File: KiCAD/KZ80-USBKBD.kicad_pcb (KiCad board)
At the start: 2 copper layers, 100 x 75 mm, 33 parts, among them J1 SBC8080 BUS, J2 CON-A, J3 CMT-OUT, J4 232C(DEBUG), J5 ADR-JP2, J6 ADR-JP1, SW1 SW_SPST, U1 Pico, U2 8255, U3 74HC139, U4 74HC00

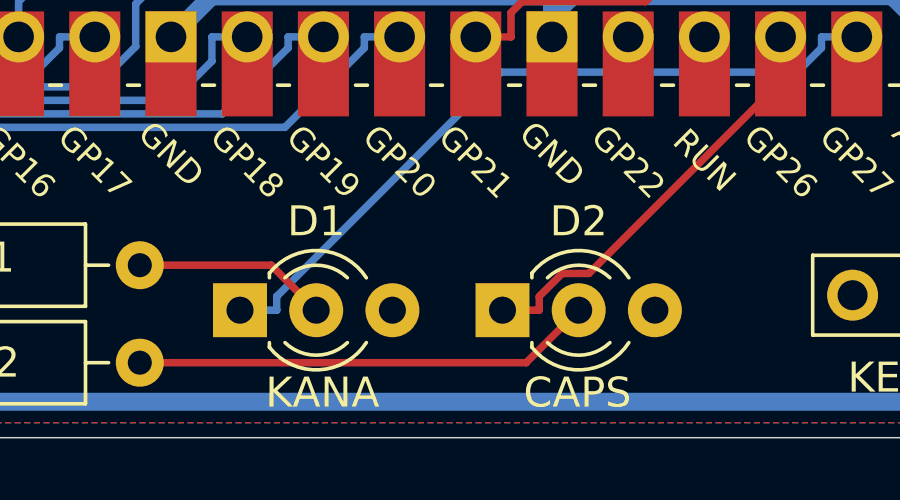
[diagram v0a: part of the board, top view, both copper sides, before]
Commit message: LEDフットプリント間違い修正
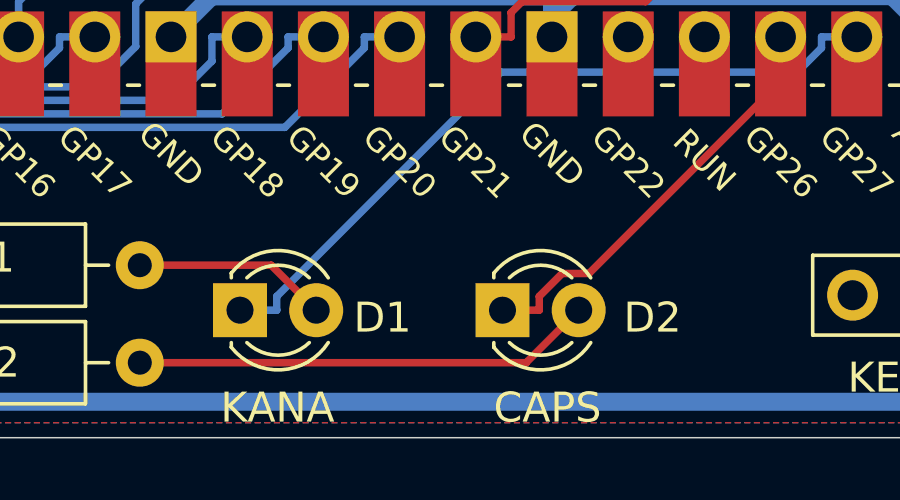
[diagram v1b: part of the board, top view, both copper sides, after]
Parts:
- D1, D2: footprint LED_THT:LED_D3.0mm-3 -> LED_THT:LED_D3.0mm
- R6, R7, R8, R9: value 1k -> 10k
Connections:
- J1 pad 18: Net-(J1-Pad18) -> (no net)
- J1 pad 20: Net-(J1-Pad20) -> (no net)
- J1 pad 22: Net-(J1-Pad22) -> (no net)
- J1 pad 23: Net-(J1-Pad23) -> (no net)
- J1 pad 24: Net-(J1-Pad24) -> (no net)
- J1 pad 27: Net-(J1-Pad27) -> (no net)
- J1 pad 33: Net-(J1-Pad33) -> (no net)
- J1 pad 34: Net-(J1-Pad34) -> (no net)
- J1 pad 35: Net-(J1-Pad35) -> (no net)
- J1 pad 36: Net-(J1-Pad36) -> (no net)
- J1 pad 37: Net-(J1-Pad37) -> (no net)
- J1 pad 38: Net-(J1-Pad38) -> (no net)
- J1 pad 39: Net-(J1-Pad39) -> (no net)
- J1 pad 40: Net-(J1-Pad40) -> (no net)
- J1 pad 5: Net-(J1-Pad5) -> (no net)
- J1 pad 6: Net-(J1-Pad6) -> (no net)
- J1 pad 7: Net-(J1-Pad7) -> (no net)
- J1 pad 8: Net-(J1-Pad8) -> (no net)
- J3 pad 2: Net-(J3-Pad2) -> (no net)
- J3 pad 3: Net-(J3-Pad3) -> (no net)
- J3 pad 4: Net-(J3-Pad4) -> (no net)
- J4 pad 2: Net-(J4-Pad2) -> (no net)
- J4 pad 3: Net-(J4-Pad3) -> (no net)
- J4 pad 6: Net-(J4-Pad6) -> (no net)

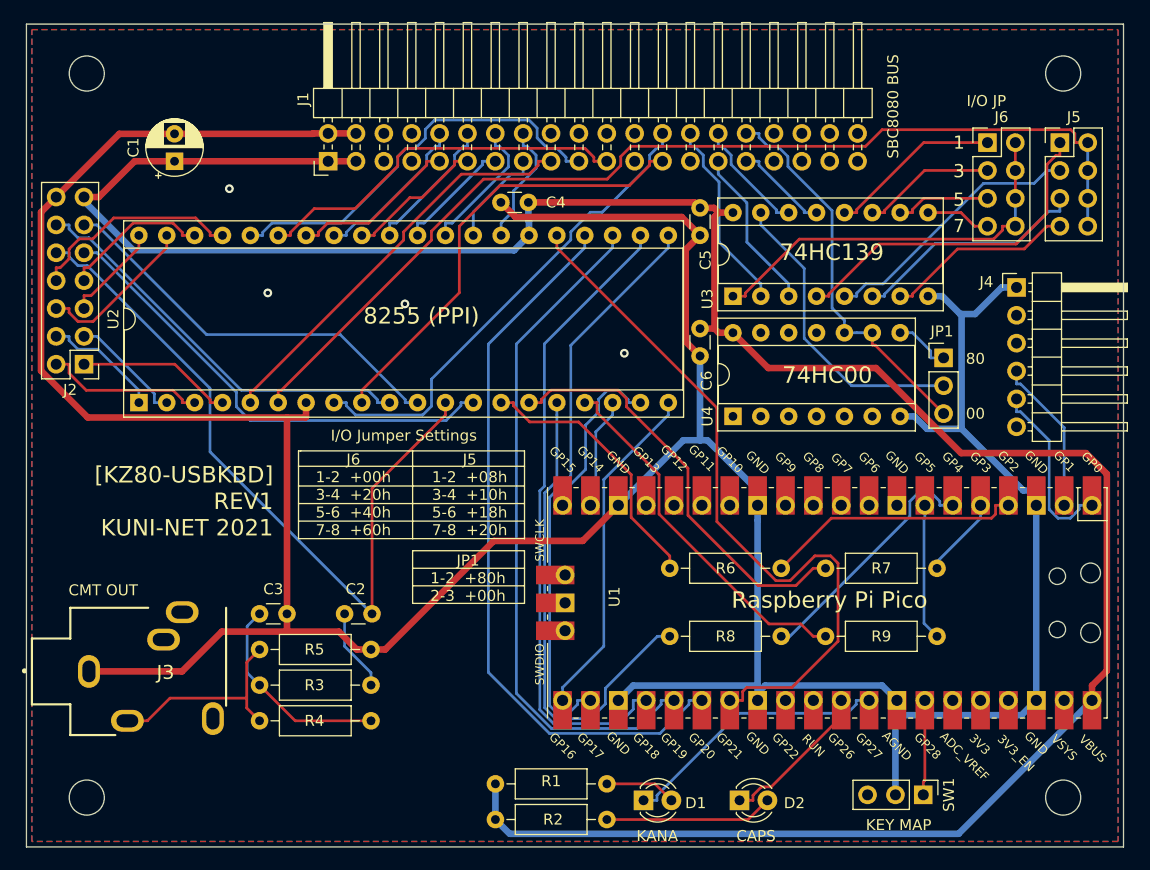
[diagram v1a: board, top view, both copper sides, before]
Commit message: REV1基板バグ対応、REV2作成、ガーバー出力
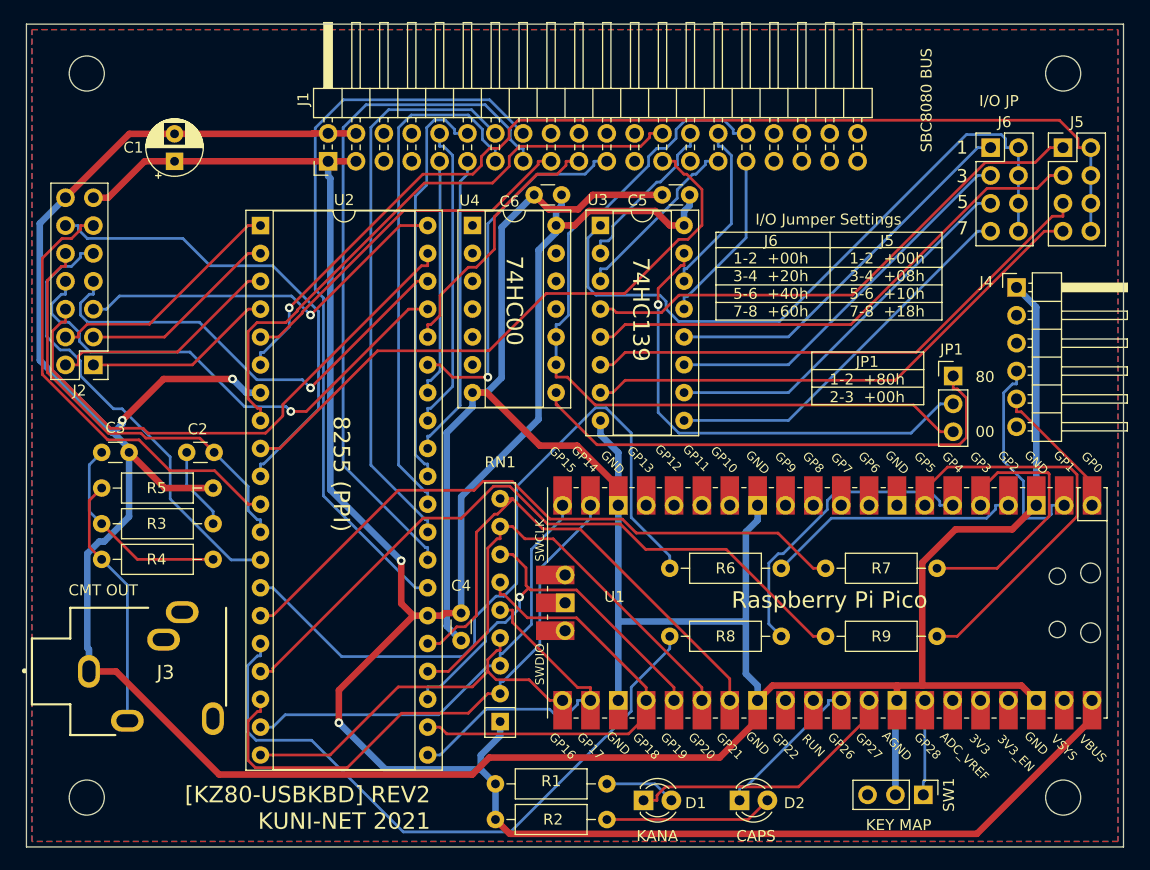
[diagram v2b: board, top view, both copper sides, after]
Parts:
- added RN1: chB-PullUP, Resistor_THT:R_Array_SIP9, F.Cu at (135.2, 117.6)
- C3: value 0.0022u -> 0.022u
- moved C4 40.1 mm to (131.6, 110.2), turned to 90 degrees
- moved U4 29.4 mm to (132.7, 72.3), turned to 0 degrees
- moved C2 20.6 mm to (106.6, 93.0)
- moved C3 20.6 mm to (98.9, 93.0)
- moved R3 20.6 mm to (98.9, 99.5)
- moved R4 20.6 mm to (98.9, 102.8)
- moved R5 20.6 mm to (98.9, 96.3)
- moved U2 19.6 mm to (113.3, 72.4), turned to 0 degrees
- moved C6 17.5 mm to (140.8, 69.6), turned to 180 degrees
- moved U3 13.7 mm to (144.3, 72.3), turned to 0 degrees
- moved JP1 1.87 mm to (176.5, 86.1)
- moved C5 1.52 mm to (152.5, 69.6), turned to 180 degrees
- moved J2 0.85 mm to (98.1, 85.1)
- moved J5 0.54 mm to (186.5, 65.3)
- moved J6 0.54 mm to (179.9, 65.3)
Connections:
- net ~IORD renamed ~{IORD}
- net ~IOWR renamed ~{IOWR}
- J1 pad 18: (no net) -> unconnected-(J1-Pad18)
- J1 pad 20: (no net) -> unconnected-(J1-Pad20)
- J1 pad 22: (no net) -> unconnected-(J1-Pad22)
- J1 pad 23: (no net) -> unconnected-(J1-Pad23)
- J1 pad 24: (no net) -> unconnected-(J1-Pad24)
- J1 pad 27: (no net) -> unconnected-(J1-Pad27)
- J1 pad 33: (no net) -> unconnected-(J1-Pad33)
- J1 pad 34: (no net) -> unconnected-(J1-Pad34)
- J1 pad 35: (no net) -> unconnected-(J1-Pad35)
- J1 pad 36: (no net) -> unconnected-(J1-Pad36)
- J1 pad 37: (no net) -> unconnected-(J1-Pad37)
- J1 pad 38: (no net) -> unconnected-(J1-Pad38)
- J1 pad 39: (no net) -> unconnected-(J1-Pad39)
- J1 pad 40: (no net) -> unconnected-(J1-Pad40)
- J1 pad 5: (no net) -> unconnected-(J1-Pad5)
- J1 pad 6: (no net) -> unconnected-(J1-Pad6)
- J1 pad 7: (no net) -> unconnected-(J1-Pad7)
- J1 pad 8: (no net) -> unconnected-(J1-Pad8)
- J3 pad 2: (no net) -> unconnected-(J3-Pad2)
- J3 pad 3: (no net) -> unconnected-(J3-Pad3)
- J3 pad 4: (no net) -> unconnected-(J3-Pad4)
- J4 pad 2: (no net) -> unconnected-(J4-Pad2)
- J4 pad 3: (no net) -> unconnected-(J4-Pad3)
- J4 pad 6: (no net) -> unconnected-(J4-Pad6)
- U1 pad 10: Net-(U1-Pad10) -> unconnected-(U1-Pad10)
- U1 pad 11: Net-(U1-Pad11) -> unconnected-(U1-Pad11)
- U1 pad 12: Net-(U1-Pad12) -> unconnected-(U1-Pad12)
- U1 pad 14: Net-(U1-Pad14) -> unconnected-(U1-Pad14)
- U1 pad 15: Net-(U1-Pad15) -> unconnected-(U1-Pad15)
- U1 pad 16: Net-(U1-Pad16) -> unconnected-(U1-Pad16)
- U1 pad 17: Net-(U1-Pad17) -> unconnected-(U1-Pad17)
- U1 pad 29: Net-(U1-Pad29) -> unconnected-(U1-Pad29)
- U1 pad 30: Net-(U1-Pad30) -> unconnected-(U1-Pad30)
- U1 pad 35: Net-(U1-Pad35) -> unconnected-(U1-Pad35)
- U1 pad 36: Net-(U1-Pad36) -> unconnected-(U1-Pad36)
- U1 pad 37: Net-(U1-Pad37) -> unconnected-(U1-Pad37)
- U1 pad 39: Net-(U1-Pad39) -> unconnected-(U1-Pad39)
- U1 pad 41: Net-(U1-Pad41) -> unconnected-(U1-Pad41)
- U1 pad 42: Net-(U1-Pad42) -> unconnected-(U1-Pad42)
- U1 pad 43: Net-(U1-Pad43) -> unconnected-(U1-Pad43)
- U1 pad 8: Net-(U1-Pad8) -> unconnected-(U1-Pad8)
- U1 pad 9: Net-(U1-Pad9) -> unconnected-(U1-Pad9)
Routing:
- net GND: track 327.4 -> 386.1 mm, vias 4 -> 2
- net /D7: track 11.3 -> 68.1 mm
- net /D6: track 9.29 -> 63.3 mm
- net /X0: track 10.2 -> 53.0 mm
- net /Y0: track 24.7 -> 67.1 mm
- net Net-(JP1-Pad1): track 5.28 -> 46.6 mm
- net /D5: track 12.8 -> 52.1 mm
- net /A7: track 35.8 -> 74.1 mm
- net /D4: track 10.7 -> 47.8 mm
- net /PA5: track 14.7 -> 50.9 mm
- net Net-(J5-Pad7): track 17.3 -> 48.3 mm
- net /Y3: track 33.4 -> 64.3 mm
- net Net-(J6-Pad7): track 5.93 -> 35.1 mm
- net /PC5: track 68.1 -> 39.1 mm
- net /PA6: track 13.6 -> 42.3 mm, vias 0 -> 1
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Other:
- net class BOLD removed
- net class Default removed
- board text added: "J5 1-2 +00h 3-4 +08h 5-6 +10h 7-8 +18h"
- board text added: "[KZ80-USBKBD] REV2 KUNI-NET 2021"
- board text removed: "J5 1-2 +08h 3-4 +10h 5-6 +18h 7-8 +20h"
- board text removed: "[KZ80-USBKBD] REV1 KUNI-NET 2021"

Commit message: REV2 基板 回路不足部分追加・パターン修正・ガーバー再出力
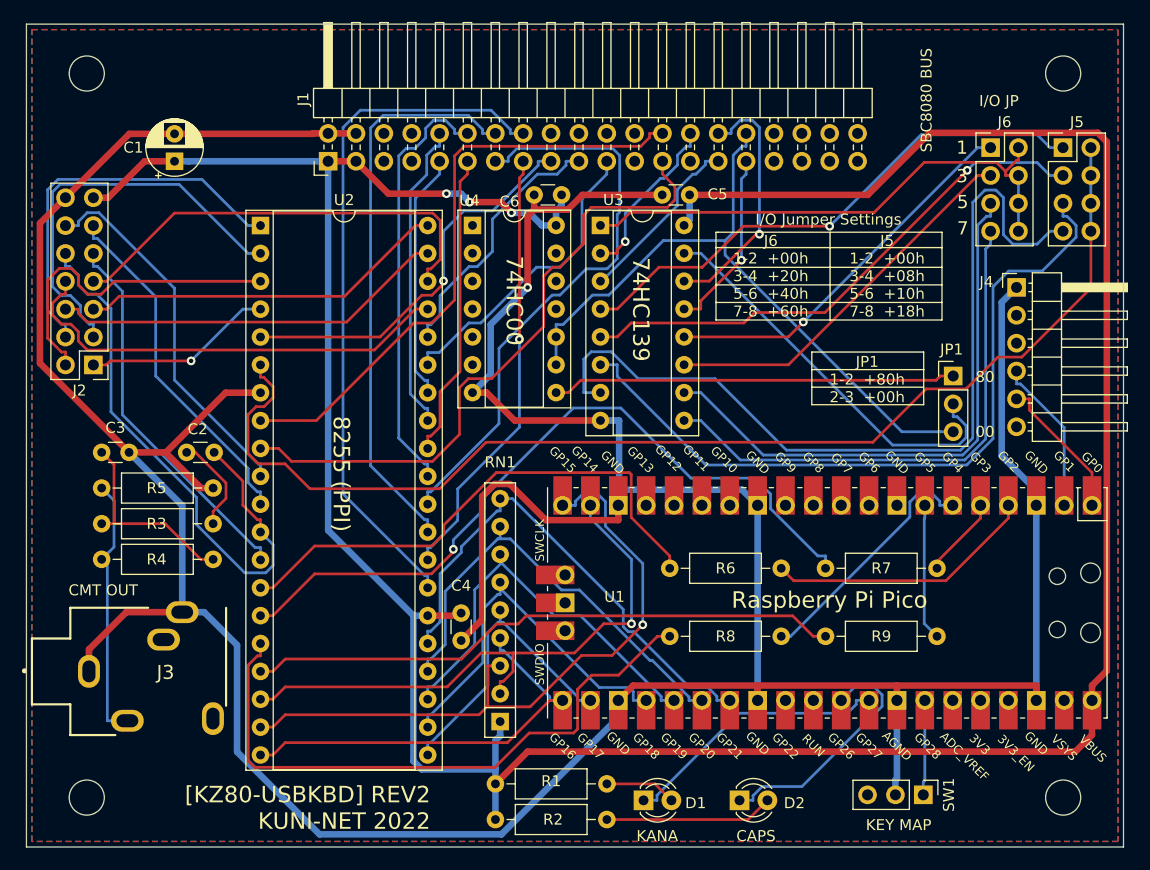
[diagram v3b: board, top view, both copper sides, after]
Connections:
- J3 pad 2: unconnected-(J3-Pad2) -> GND
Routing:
- net VCC: track 230.5 -> 282.8 mm, vias 2 -> 3
- net Net-(J5-Pad7): track 48.3 -> 79.2 mm
- net Net-(R9-Pad1): track 37.5 -> 12.4 mm
- net /D6: track 63.3 -> 40.1 mm, vias 0 -> 1
- net /X1: track 41.3 -> 61.2 mm, vias 0 -> 1
- net Net-(J5-Pad5): track 48.9 -> 68.3 mm
- net /PA2: track 18.4 -> 37.3 mm
- net /Y0: track 67.1 -> 48.7 mm
- net Net-(R7-Pad1): track 24.4 -> 7.38 mm
- net Net-(J6-Pad5): track 35.1 -> 52.0 mm
- net GND: track 386.1 -> 370.9 mm, vias 2 -> 1
- net /PA5: track 50.9 -> 36.3 mm
- net Net-(J6-Pad7): track 35.1 -> 48.9 mm
- net /PA3: track 22.2 -> 35.8 mm
- net Net-(J6-Pad2): track 62.7 -> 49.0 mm
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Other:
- board text added: "[KZ80-USBKBD] REV2 KUNI-NET 2022"
- board text removed: "[KZ80-USBKBD] REV2 KUNI-NET 2021"
